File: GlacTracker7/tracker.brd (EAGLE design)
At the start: 120 x 89.3 mm, 91 parts, among them J1 THING_PLUS_PHYSICAL, Q1 2N3906, Q2 DMG6602SVT, Q3 DMG6602SVT, Q6 MMBT3906LT1SMD, Q7 DMG6602SVT, U1 ADXL343BCCZ-RL7, U2 FONA-800-BREAKOUTNOHOLE, U3 MP2155GQ-Z, U4 SPARKFUN-SWARM-M138NOTOPHOLE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

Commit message: Add BatVolts divider values
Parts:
- R24: value 200R 0.1% -> 680K 0.1%
- R25: value 1K 0.1% -> 330K 0.1%
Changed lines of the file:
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@@
 <attribute name="VALUE" x="45.847" y="13.081" size="1.27" layer="27" rot="R270"/>
 </element>
-<element name="R24" library="resistor" package="R0805" value="200R 0.1%" x="117.094" y="20.066" smashed="yes">
+<element name="R24" library="resistor" package="R0805" value="680K 0.1%" x="117.094" y="20.066" smashed="yes">
 <attribute name="NAME" x="117.094" y="19.05" size="0.889" layer="25" rot="R180" align="bottom-center"/>
 <attribute name="VALUE" x="116.332" y="17.78" size="1.27" layer="27"/>
 </element>
-<element name="R25" library="resistor" package="R0805" value="1K 0.1%" x="117.094" y="16.764" smashed="yes" rot="R180">
+<element name="R25" library="resistor" package="R0805" value="330K 0.1%" x="117.094" y="16.764" smashed="yes" rot="R180">
 <attribute name="NAME" x="117.094" y="15.748" size="0.889" layer="25" rot="R180" align="bottom-center"/>
 <attribute name="VALUE" x="117.856" y="19.05" size="1.27" layer="27" rot="R180"/>

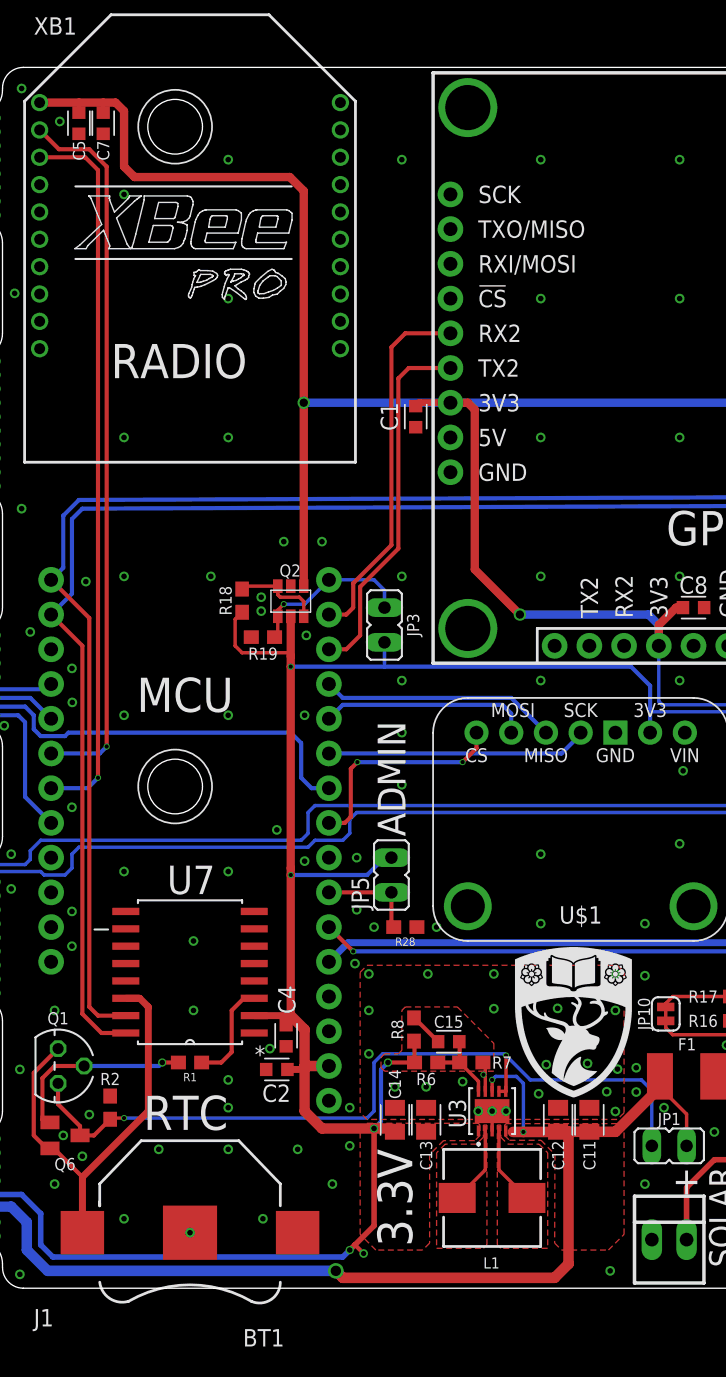
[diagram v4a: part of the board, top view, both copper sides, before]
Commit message: update the silkscreen
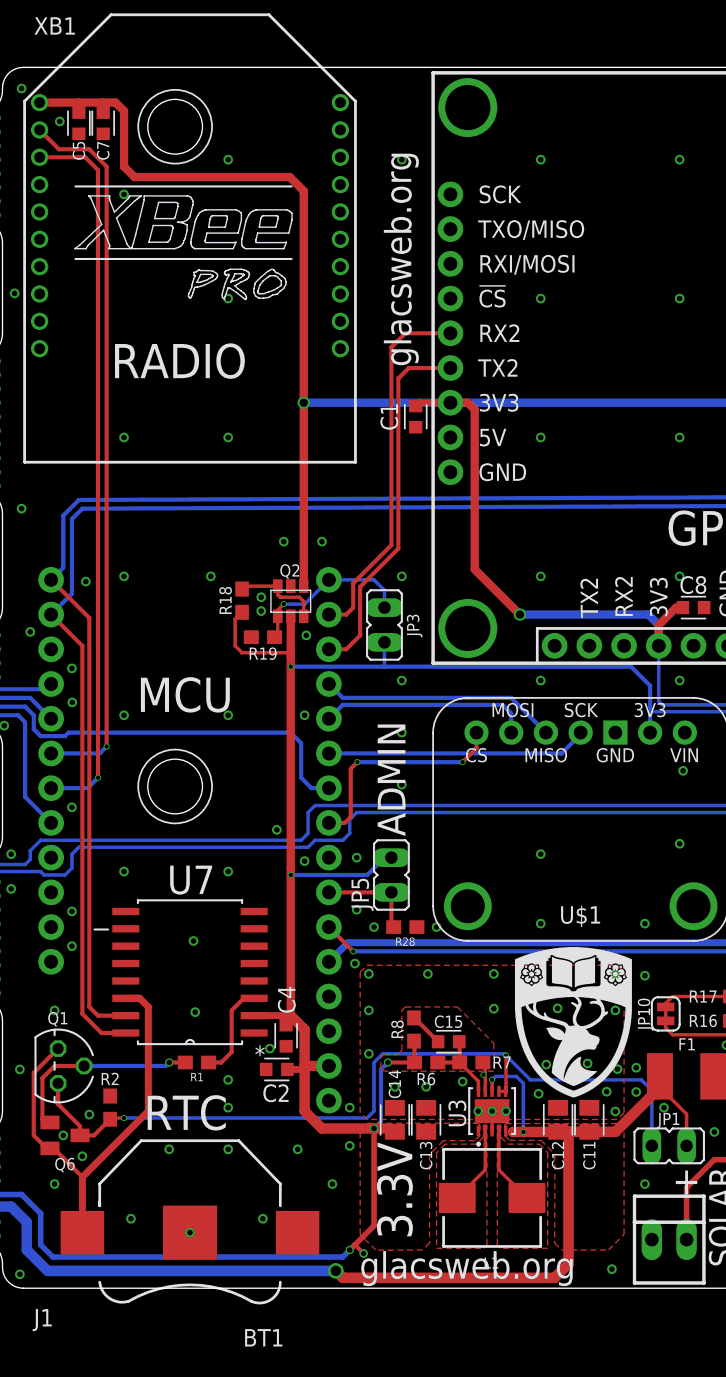
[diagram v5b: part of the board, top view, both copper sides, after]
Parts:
- moved R1 0.51 mm to (58.7, 16.5)
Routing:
- net RTC_!INT: track 7.58 -> 7.07 mm
- net N$2: track 14.1 -> 14.6 mm
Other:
- board text added: "I am a piece of scientific equipment for glacier monitoring."
- board text added: "If you can read this, I am broken. Please visit: http://glacsweb.org"
- board text added: "glacsweb.org"
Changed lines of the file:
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@@
 <setting verticaltext="up"/>
 </settings>
-<grid distance="10" unitdist="mil" unit="mil" style="lines" multiple="1" display="yes" altdistance="0.5" altunitdist="mil" altunit="mil"/>
+<grid distance="10" unitdist="mil" unit="mil" style="lines" multiple="1" display="yes" altdistance="5" altunitdist="mil" altunit="mil"/>
 <layers>
-<layer number="1" name="Top" color="4" fill="1" visible="yes" active="yes"/>
+<layer number="1" name="Top" color="4" fill="1" visible="no" active="yes"/>
 <layer number="2" name="Route2" color="16" fill="1" visible="no" active="no"/>
 <layer number="3" name="Route3" color="17" fill="1" visible="no" active="no"/>
@@
 <layer number="19" name="Unrouted" color="6" fill="1" visible="yes" active="yes"/>
 <layer number="20" name="Dimension" color="24" fill="1" visible="yes" active="yes"/>
-<layer number="21" name="tPlace" color="7" fill="1" visible="yes" active="yes"/>
-<layer number="22" name="bPlace" color="7" fill="1" visible="no" active="yes"/>
-<layer number="23" name="tOrigins" color="15" fill="1" visible="yes" active="yes"/>
-<layer number="24" name="bOrigins" color="15" fill="1" visible="no" active="yes"/>
-<layer number="25" name="tNames" color="7" fill="1" visible="yes" active="yes"/>
-<layer number="26" name="bNames" color="7" fill="1" visible="no" active="yes"/>
+<layer number="21" name="tPlace" color="7" fill="1" visible="no" active="yes"/>
+<layer number="22" name="bPlace" color="7" fill="1" visible="yes" active="yes"/>
+<layer number="23" name="tOrigins" color="15" fill="1" visible="no" active="yes"/>
+<layer number="24" name="bOrigins" color="15" fill="1" visible="yes" active="yes"/>
+<layer number="25" name="tNames" color="7" fill="1" visible="no" active="yes"/>
+<layer number="26" name="bNames" color="7" fill="1" visible="yes" active="yes"/>
 <layer number="27" name="tValues" color="7" fill="1" visible="no" active="yes"/>
 <layer number="28" name="bValues" color="7" fill="1" visible="no" active="yes"/>
@@
 <layer number="37" name="tTest" color="7" fill="1" visible="no" active="yes"/>
 <layer number="38" name="bTest" color="7" fill="1" visible="no" active="yes"/>
-<layer number="39" name="tKeepout" color="4" fill="11" visible="yes" active="yes"/>
-<layer number="40" name="bKeepout" color="1" fill="11" visible="no" active="yes"/>
-<layer number="41" name="tRestrict" color="4" fill="10" visible="yes" active="yes"/>
-<layer number="42" name="bRestrict" color="1" fill="10" visible="no" active="yes"/>
+<layer number="39" name="tKeepout" color="4" fill="11" visible="no" active="yes"/>
+<layer number="40" name="bKeepout" color="1" fill="11" visible="yes" active="yes"/>
+<layer number="41" name="tRestrict" color="4" fill="10" visible="no" active="yes"/>
+<layer number="42" name="bRestrict" color="1" fill="10" visible="yes" active="yes"/>
 <layer number="43" name="vRestrict" color="2" fill="10" visible="no" active="yes"/>
 <layer number="44" name="Drills" color="7" fill="1" visible="yes" active="yes"/>
@@
 <layer number="49" name="Reference" color="7" fill="1" visible="no" active="yes"/>
 <layer number="50" name="dxf" color="7" fill="1" visible="no" active="no"/>
-<layer number="51" name="tDocu" color="7" fill="1" visible="yes" active="yes"/>
-<layer number="52" name="bDocu" color="7" fill="1" visible="no" active="yes"/>
+<layer number="51" name="tDocu" color="7" fill="1" visible="no" active="yes"/>
+<layer number="52" name="bDocu" color="7" fill="1" visible="yes" active="yes"/>
 <layer number="53" name="tGND_GNDA" color="7" fill="9" visible="no" active="no"/>
 <layer number="54" name="bGND_GNDA" color="1" fill="9" visible="no" active="no"/>
@@
 <text x="94.488" y="6.858" size="2.032" layer="25" align="bottom-center">+</text>
 <text x="113.03" y="12.7" size="2.032" layer="25" align="bottom-center">+</text>
-<text x="74.422" y="3.048" size="2.54" layer="21" ratio="15" rot="R90">3.3V</text>
+<text x="74.422" y="3.556" size="2.54" layer="21" ratio="15" rot="R90">3.3V</text>
 <text x="11.938" y="4.572" size="2.54" layer="21" ratio="15" rot="R90">4.4V</text>
 <wire x1="44.45" y1="87.776" x2="44.45" y2="87.63" width="0" layer="20"/>
@@
 <text x="98.242" y="28.896" size="4.5" layer="25" font="vector" ratio="15">IT3</text>
 <text x="98.242" y="25.848" size="2.54" layer="25" font="vector" ratio="15">V1.0</text>
-<text x="115.366" y="20.749" size="2.1844" layer="22" font="fixed" rot="MR0">Graeme Bragg
+<text x="120.221" y="37.388" size="2.1844" layer="22" font="fixed" rot="MR270">Graeme Bragg
 Kirk Martinez
 Sherif Attia
@@
 <rectangle x1="85.897721875" y1="24.94788125" x2="86.537796875" y2="24.9580375" layer="21"/>
 <text x="72.908" y="33.056" size="2.032" layer="21" ratio="15" rot="R90" align="center-left">ADMIN</text>
+<text x="70.556" y="0.702" size="1.9304" layer="25" font="vector" ratio="15">glacsweb.org</text>
+<text x="74.355" y="67.381" size="1.9304" layer="25" font="vector" ratio="15" rot="R90">glacsweb.org</text>
+<text x="82.217" y="1.982" size="2.1844" layer="22" font="fixed" rot="MR90">I am a piece of
+scientific equipment
+for glacier monitoring.</text>
+<text x="51.483" y="0.712" size="2.1844" layer="22" font="fixed" rot="MR90">If you can read this,
+I am broken.
+Please visit:
+http://glacsweb.org</text>
 </plain>
 <attributes>
@@
 <attribute name="VALUE" x="47.244" y="13.081" size="1.27" layer="27" ratio="10" rot="R270"/>
 </element>
-<element name="R1" library="SparkFun-Resistors" package="0603" value="100k" x="58.166" y="16.51" smashed="yes" rot="R180">
-<attribute name="NAME" x="58.166" y="15.748" size="0.6096" layer="25" font="vector" ratio="20" rot="R180" align="bottom-center"/>
-<attribute name="PROD_ID" value=" " x="58.166" y="16.51" size="1.778" layer="27" rot="R180" display="off"/>
-<attribute name="VALUE" x="58.166" y="17.272" size="0.6096" layer="27" font="vector" ratio="20" rot="R180" align="top-center"/>
+<element name="R1" library="SparkFun-Resistors" package="0603" value="100k" x="58.674" y="16.51" smashed="yes" rot="R180">
+<attribute name="NAME" x="58.674" y="15.748" size="0.6096" layer="25" font="vector" ratio="20" rot="R180" align="bottom-center"/>
+<attribute name="PROD_ID" value=" " x="58.674" y="16.51" size="1.778" layer="27" rot="R180" display="off"/>
+<attribute name="VALUE" x="58.674" y="17.272" size="0.6096" layer="27" font="vector" ratio="20" rot="R180" align="top-center"/>
 </element>
 <element name="3.3V" library="led" package="CHIP-LED0805" value="" x="111.506" y="41.91" smashed="yes" rot="R270">
@@
 <via x="106.68" y="5.08" extent="1-16" drill="0.4064" diameter="0.7112"/>
 <via x="91.44" y="7.62" extent="1-16" drill="0.4064" diameter="0.7112"/>
-<via x="88.9" y="1.27" extent="1-16" drill="0.4064" diameter="0.7112"/>
+<via x="89.027" y="1.397" extent="1-16" drill="0.4064" diameter="0.7112"/>
 <via x="60.96" y="72.39" extent="1-16" drill="0.4064" diameter="0.7112"/>
 <via x="60.96" y="62.23" extent="1-16" drill="0.4064" diameter="0.7112"/>
@@
 <via x="60.96" y="15.24" extent="1-16" drill="0.4064" diameter="0.7112"/>
 <via x="60.96" y="10.16" extent="1-16" drill="0.4064" diameter="0.7112"/>
-<via x="55.88" y="10.16" extent="1-16" drill="0.4064" diameter="0.7112"/>
+<via x="56.642" y="10.16" extent="1-16" drill="0.4064" diameter="0.7112"/>
 <via x="58.42" y="25.4" extent="1-16" drill="0.4064" diameter="0.7112"/>
-<via x="58.42" y="20.32" extent="1-16" drill="0.4064" diameter="0.7112"/>
+<via x="58.547" y="20.193" extent="1-16" drill="0.4064" diameter="0.7112"/>
 <via x="48.26" y="20.32" extent="1-16" drill="0.4064" diameter="0.7112"/>
 <via x="50.8" y="12.7" extent="1-16" drill="0.4064" diameter="0.7112"/>
 <via x="48.26" y="7.62" extent="1-16" drill="0.4064" diameter="0.7112"/>
-<via x="53.34" y="5.08" extent="1-16" drill="0.4064" diameter="0.7112"/>
+<via x="53.848" y="5.08" extent="1-16" drill="0.4064" diameter="0.7112"/>
 <via x="63.5" y="5.08" extent="1-16" drill="0.4064" diameter="0.7112"/>
 <via x="66.04" y="10.16" extent="1-16" drill="0.4064" diameter="0.7112"/>
@@
 <wire x1="61.214" y1="20.32" x2="61.214" y2="17.272" width="0.3048" layer="1"/>
 <wire x1="61.214" y1="17.272" x2="60.452" y2="16.51" width="0.3048" layer="1"/>
-<wire x1="60.452" y1="16.51" x2="59.016" y2="16.51" width="0.3048" layer="1"/>
+<wire x1="60.452" y1="16.51" x2="59.524" y2="16.51" width="0.3048" layer="1"/>
 </signal>
 <signal name="RTC_BAT">
@@
 <contactref element="R1" pad="2"/>
 <contactref element="Q1" pad="2"/>
-<wire x1="55.88" y1="16.256" x2="56.134" y2="16.51" width="0.3048" layer="16"/>
-<via x="56.134" y="16.51" extent="1-16" drill="0.4064"/>
-<wire x1="56.134" y1="16.51" x2="57.316" y2="16.51" width="0.3048" layer="1"/>
+<wire x1="56.388" y1="16.256" x2="56.642" y2="16.51" width="0.3048" layer="16"/>
+<via x="56.642" y="16.51" extent="1-16" drill="0.4064"/>
+<wire x1="56.642" y1="16.51" x2="57.824" y2="16.51" width="0.3048" layer="1"/>
 <wire x1="50.419" y1="16.256" x2="48.26" y2="16.256" width="0.3048" layer="1"/>
 <wire x1="48.26" y1="16.256" x2="47.371" y2="15.367" width="0.3048" layer="1"/>
@@
 <wire x1="47.498" y1="12.192" x2="47.856" y2="12.192" width="0.3048" layer="1"/>
 <wire x1="47.856" y1="12.192" x2="47.922" y2="12.126" width="0.3048" layer="1"/>
-<wire x1="55.88" y1="16.256" x2="50.419" y2="16.256" width="0.3048" layer="16"/>
+<wire x1="56.388" y1="16.256" x2="50.419" y2="16.256" width="0.3048" layer="16"/>
 </signal>
 <signal name="VCC_HP2_SW1">
